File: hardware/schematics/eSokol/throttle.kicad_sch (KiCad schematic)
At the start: 20 parts, among them J2 MOT_DRV_THR, Q10 AO3400A, Q11 NPN, Q12 PNP, Q13 BC547, Q14 NPN, Q15 PNP, Q9 BC547, U7 Hall_Sensor

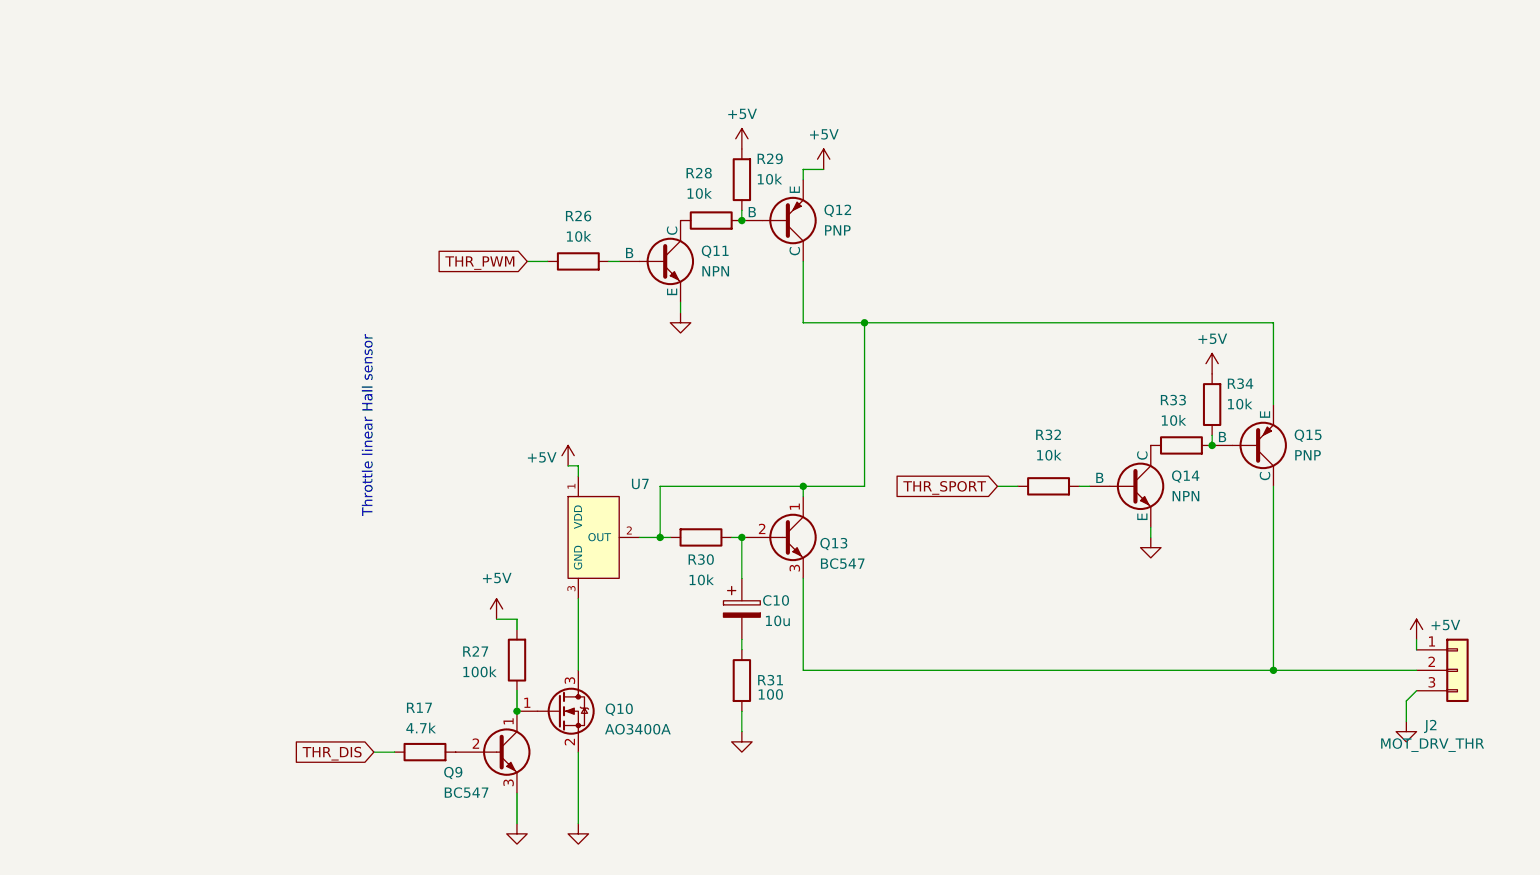
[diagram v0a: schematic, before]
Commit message: schematics: (almost) finalize throttle circuit (it's working :D), minor cleanups
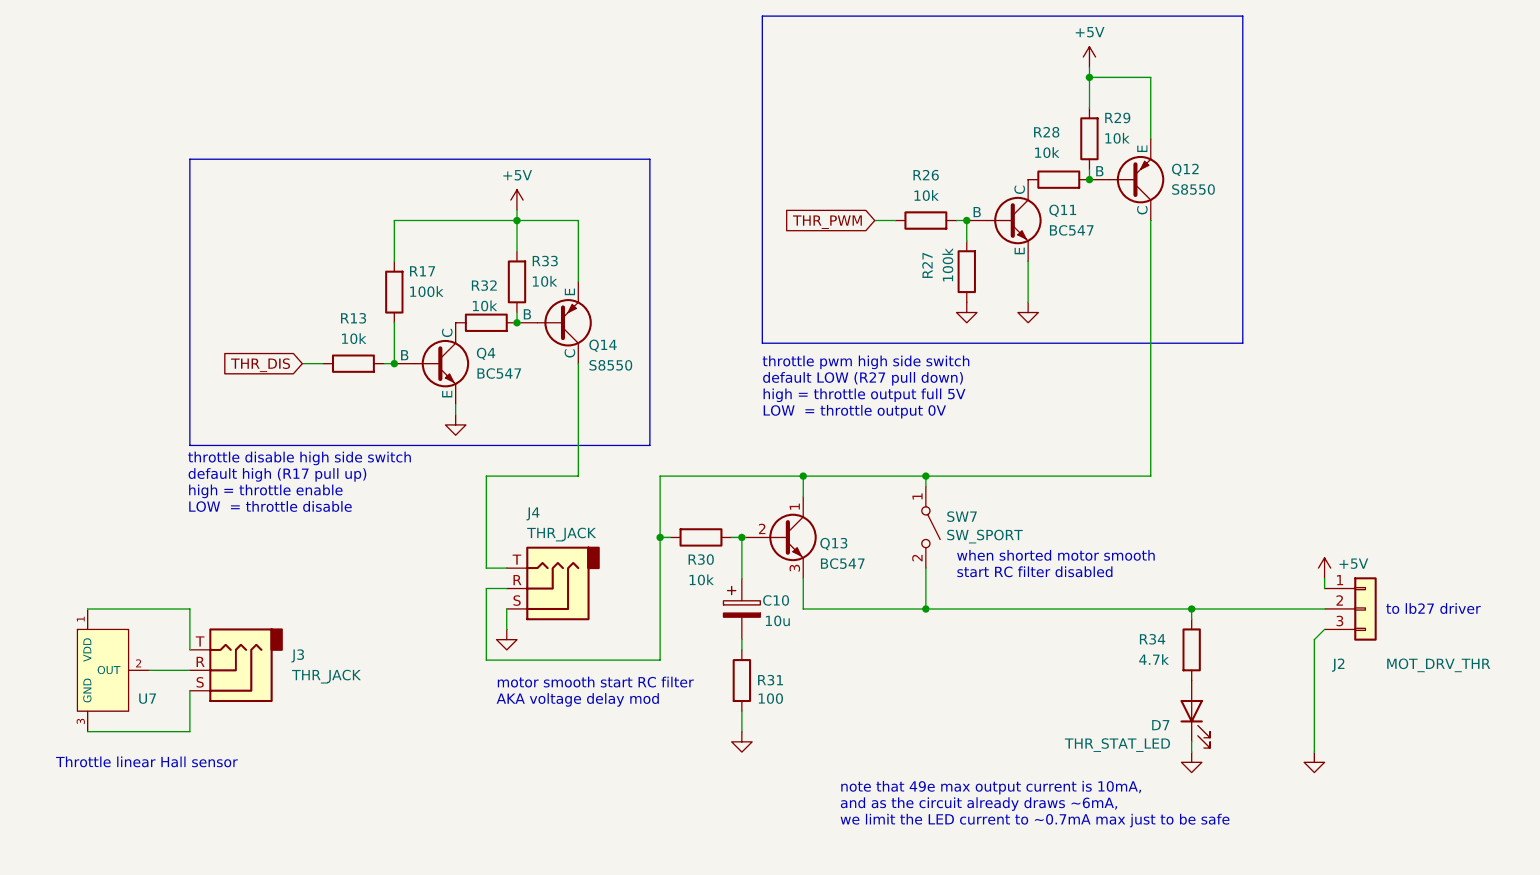
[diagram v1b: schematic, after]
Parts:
- removed Q10: AO3400A, Package_TO_SOT_SMD:SOT-23, symbol Transistor_FET:AO3400A
- removed Q14: NPN, symbol Simulation_SPICE:NPN
- removed Q15: PNP, symbol Simulation_SPICE:PNP
- removed Q9: BC547, Package_TO_SOT_THT:TO-92_Inline, symbol Transistor_BJT:BC547
- added D7: THR_STAT_LED, symbol Device:LED
- added J3, J4: THR_JACK, symbol Connector_Audio:AudioJack3
- added Q14: S8550, symbol Simulation_SPICE:PNP
- added Q4: BC547, symbol Simulation_SPICE:NPN
- added R13: 10k, symbol Device:R
- added SW7: SW_SPORT, Button_Switch_THT:SW_DIP_SPSTx01_Slide_9.78x4.72mm_W7.62mm_P2.54mm, symbol Switch:SW_SPST
- Q11: value NPN -> BC547
- Q12: value PNP -> S8550
- R17: value 4.7k -> 100k
- R34: value 10k -> 4.7k
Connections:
- net +5V: now also R17.2, R33.2, Q14.3 (E); no longer R27.2, R34.2, U7.1 (VDD)
- net GND: now also R27.1, D7.1 (K), J4.S, Q4.3 (E)
- net THR_DIS: now also R13.1; no longer R17.1
- net at Q12.1 (C), Q13.1 (C), R30.2: now also J4.R, SW7.1 (A); no longer U7.2 (OUT)
- net at U7.3 (GND): now also J3.S
- net at J2.2 (Pin_2), Q13.3 (E): now also R34.1, SW7.2 (B)
- net at Q11.2 (B), R26.2: now also R27.2
- net at R32.2: now also R33.1, Q14.2 (B)
- net THR_SPORT: no longer names the net of R32.1
- net THR_SPORT: now also Q4.1 (C)
- new net: J4.T, Q14.1 (C)
- new net: D7.2 (A), R34.2
- new net: Q4.2 (B), R13.2, R17.1
- new net: J3.R, U7.2 (OUT)
- new net: J3.T, U7.1 (VDD)
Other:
- note added: "motor smooth start RC filter AKA voltage delay mod"
- note added: "note that 49e max output current is 10mA, and as the circuit already draws ~6mA, we limit the LED current to ~0.7mA max just to be safe"
- note added: "throttle disable high side switch default high (R17 pull up) high = throttle enable LOW = throttle disable"
- note added: "throttle pwm high side switch default LOW (R27 pull down) high = throttle output full 5V LOW = throttle output 0V"
- note added: "to lb27 driver"
- note added: "when shorted motor smooth start RC filter disabled"
- moved on the sheet: J2, Q11, Q12, R26, R28, R29

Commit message: Update throttle circuits, move bigbatt to its own sheet and design ds-vc288 circuit
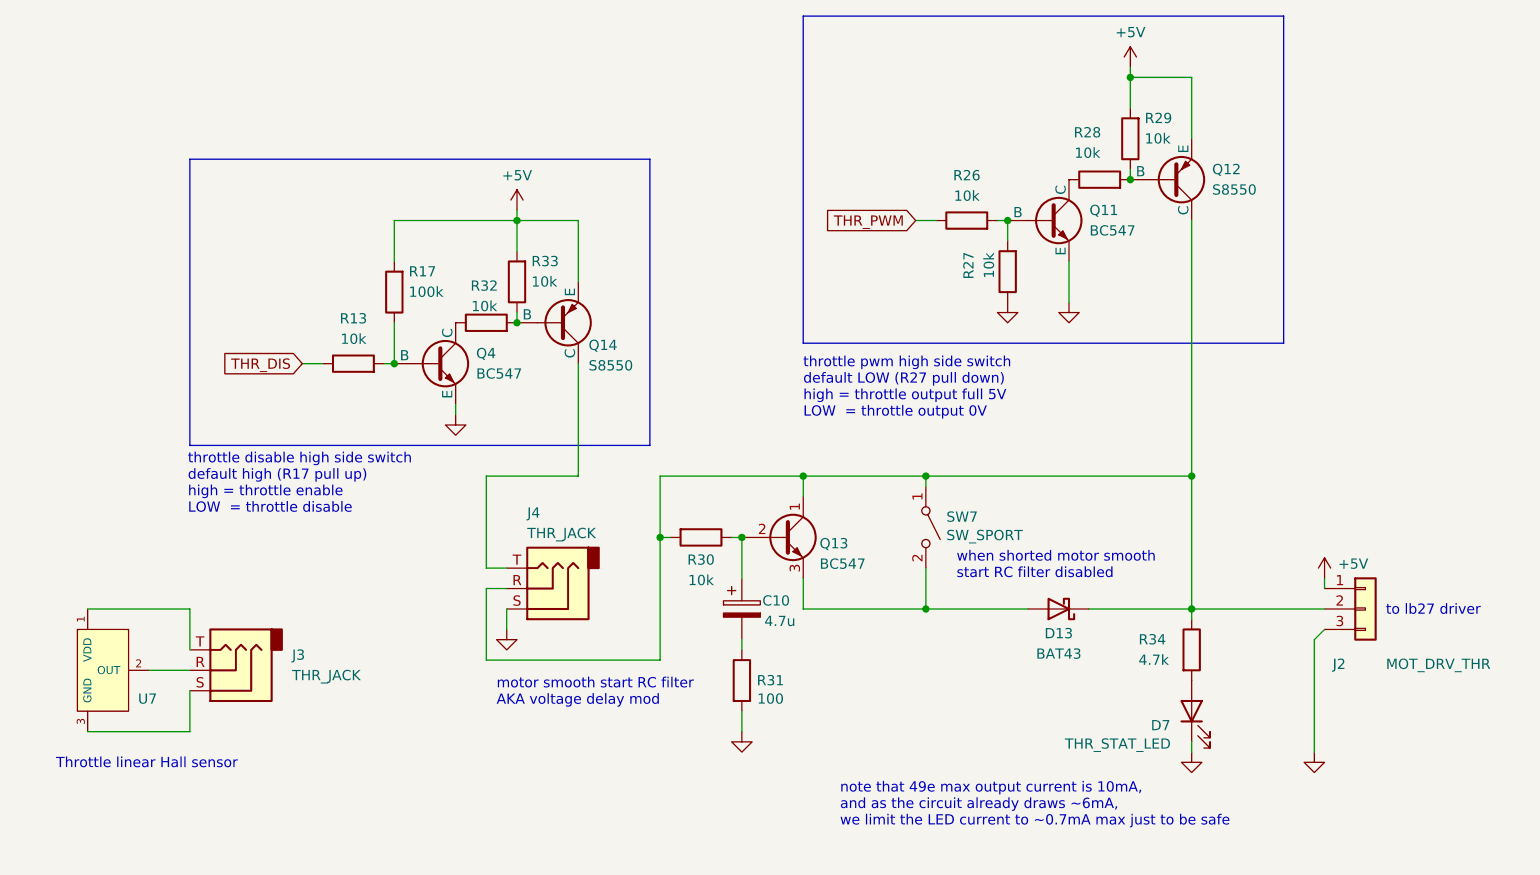
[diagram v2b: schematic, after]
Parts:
- added D13: BAT43, Diode_THT:D_DO-35_SOD27_P7.62mm_Horizontal, symbol Diode:BAT43
- C10: value 10u -> 4.7u
- R27: value 100k -> 10k
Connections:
- net at J4.R, Q12.1 (C), Q13.1 (C)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: now also J2.2 (Pin_2), R34.1, D13.1 (K)
- net at Q13.3 (E), SW7.2 (B): now also D13.2 (A); no longer J2.2 (Pin_2), R34.1
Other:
- moved on the sheet: Q11, Q12, R26, R27, R28, R29

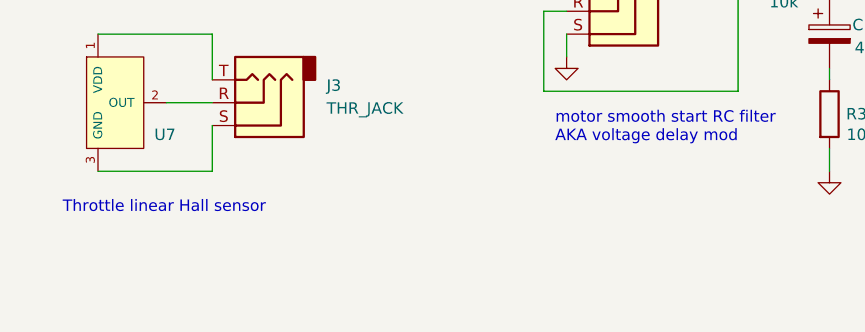
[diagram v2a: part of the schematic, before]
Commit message: Add measurements from 29.09.2024, add some todos in throttle schematics
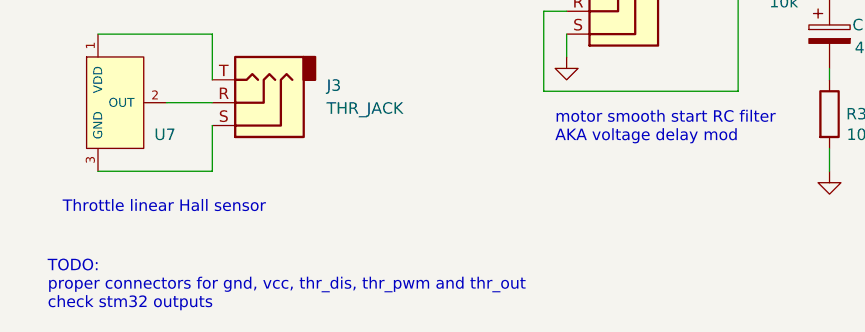
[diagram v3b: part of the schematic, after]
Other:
- note added: "TODO: proper connectors for gnd, vcc, thr_dis, thr_pwm and thr_out check stm32 outputs"
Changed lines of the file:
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@@
+		)
+	)
+	(text "TODO:\nproper connectors for gnd, vcc, thr_dis, thr_pwm and thr_out\ncheck stm32 outputs\n"
+		(exclude_from_sim no)
+		(at 21.082 130.81 0)
+		(effects
+			(font
+				(size 1.27 1.27)
+			)
+			(justify left)
 		)
 	)
